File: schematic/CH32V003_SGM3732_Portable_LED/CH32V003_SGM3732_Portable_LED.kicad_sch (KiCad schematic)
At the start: 30 parts, among them J1 USB_C_Receptacle_USB2.0_16P, Q1 CJ2301, Q2 CJ2302, SW1 SW_Push, U1 CH32V003J4M6, U2 ME6211C33M5, U3 SGM3732

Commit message: Update schematic
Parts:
- R_{CC1}: renamed from R7; value 1MΩ -> 5.1kΩ
- R_{CC2}: renamed from R6; value 1MΩ -> 5.1kΩ
- renumbered C3 to C_{LDO_IN}, C4 to C_{LDO_OUT}, C5 to C_{LED_IN}, C6 to C_{LED_OUT}, C2 to C_{MCU}, C1 to C_{P}, D4 to D1, D5 to D2, D6 to D3, D7 to D4, D8 to D5, D3 to D_{LED}, D1 to D_{Latch}, D2 to D_{Power}, L1 to L_{LED}, Q2 to NMOS, Q1 to PMOS, R5 to R_{CTRL}, R3 to R_{Latch}, R2 to R_{N}, R_led to R_{POWER}, R1 to R_{P}, SW1 to SW_{Latch}
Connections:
- net LED renamed Power_LED
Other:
- note added: "Up to 10 LEDs"

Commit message: Update readme and schematic
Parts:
- added R_{Down}: 33kΩ, symbol Device:R
- added R_{Up}: 22kΩ, symbol Device:R
- added SW_{Latch}1: SW_Push, symbol Switch:SW_Push
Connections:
- net 5V: now also R_{Up}.2
- net GND: now also R_{Down}.1, SW_{Latch}1.1
- net ADC: now reaches U1.1 (PD6/PA1)
- net ADC: now also R_{Down}.2, R_{Up}.1
- net Level_Button: now reaches U1.3 (PA2)
- net Level_Button: now also SW_{Latch}1.2
- net Latch_and_Button renamed Mode_Button
- no-connect marks 8 -> 7
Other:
- moved on the sheet: C_{MCU}, C_{P}, D_{Latch}, D_{Power}, J1, NMOS, PMOS, R_{CC1}, R_{CC2}, R_{Latch}, R_{N}, R_{POWER}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

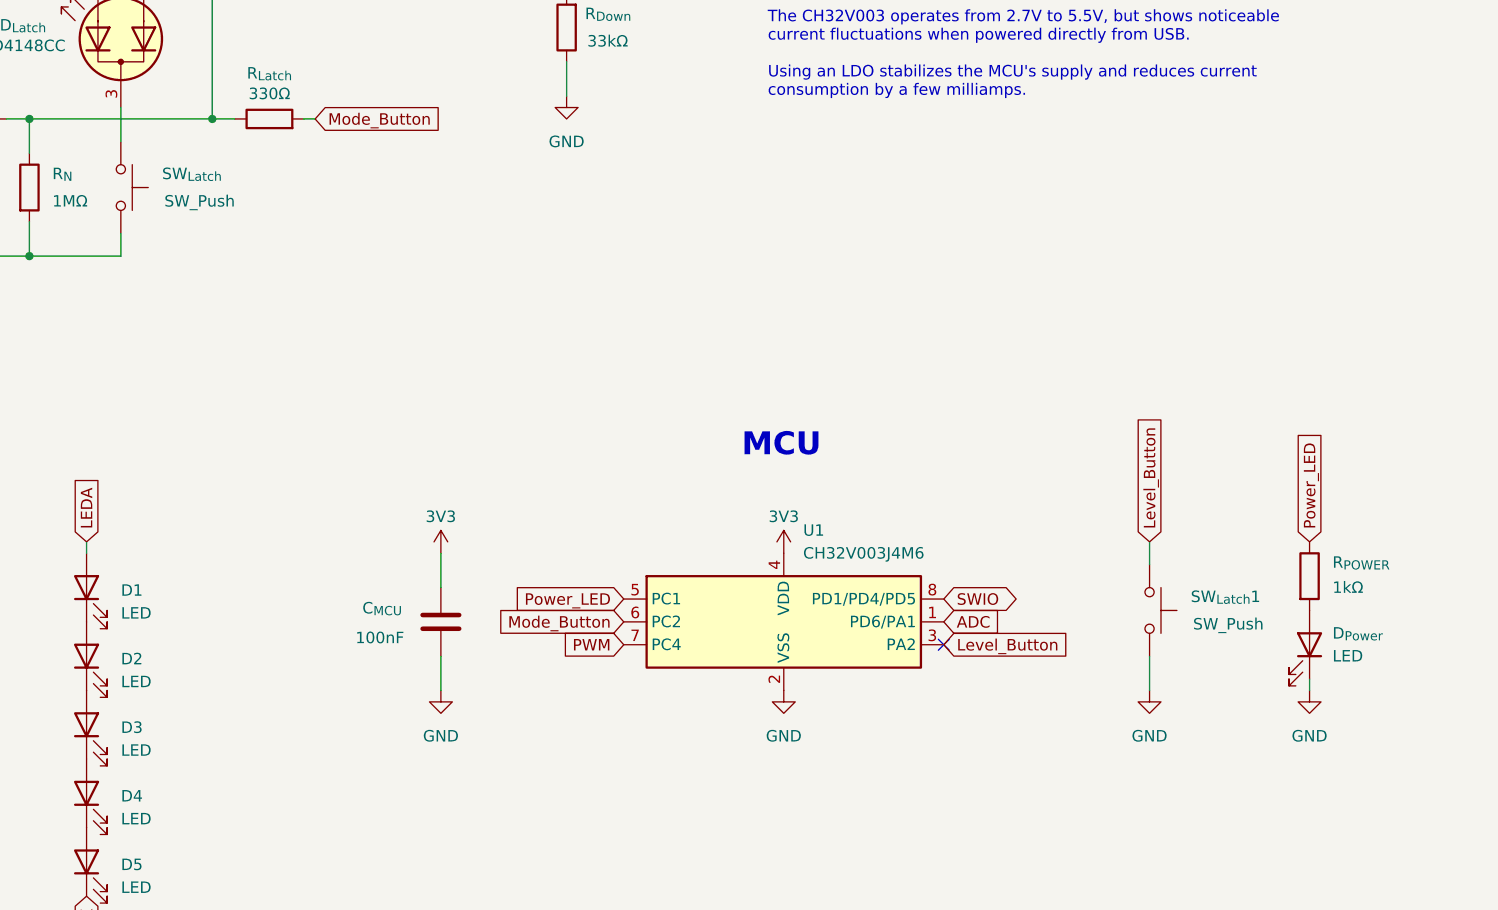
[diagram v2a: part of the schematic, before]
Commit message: Update button names in schematic
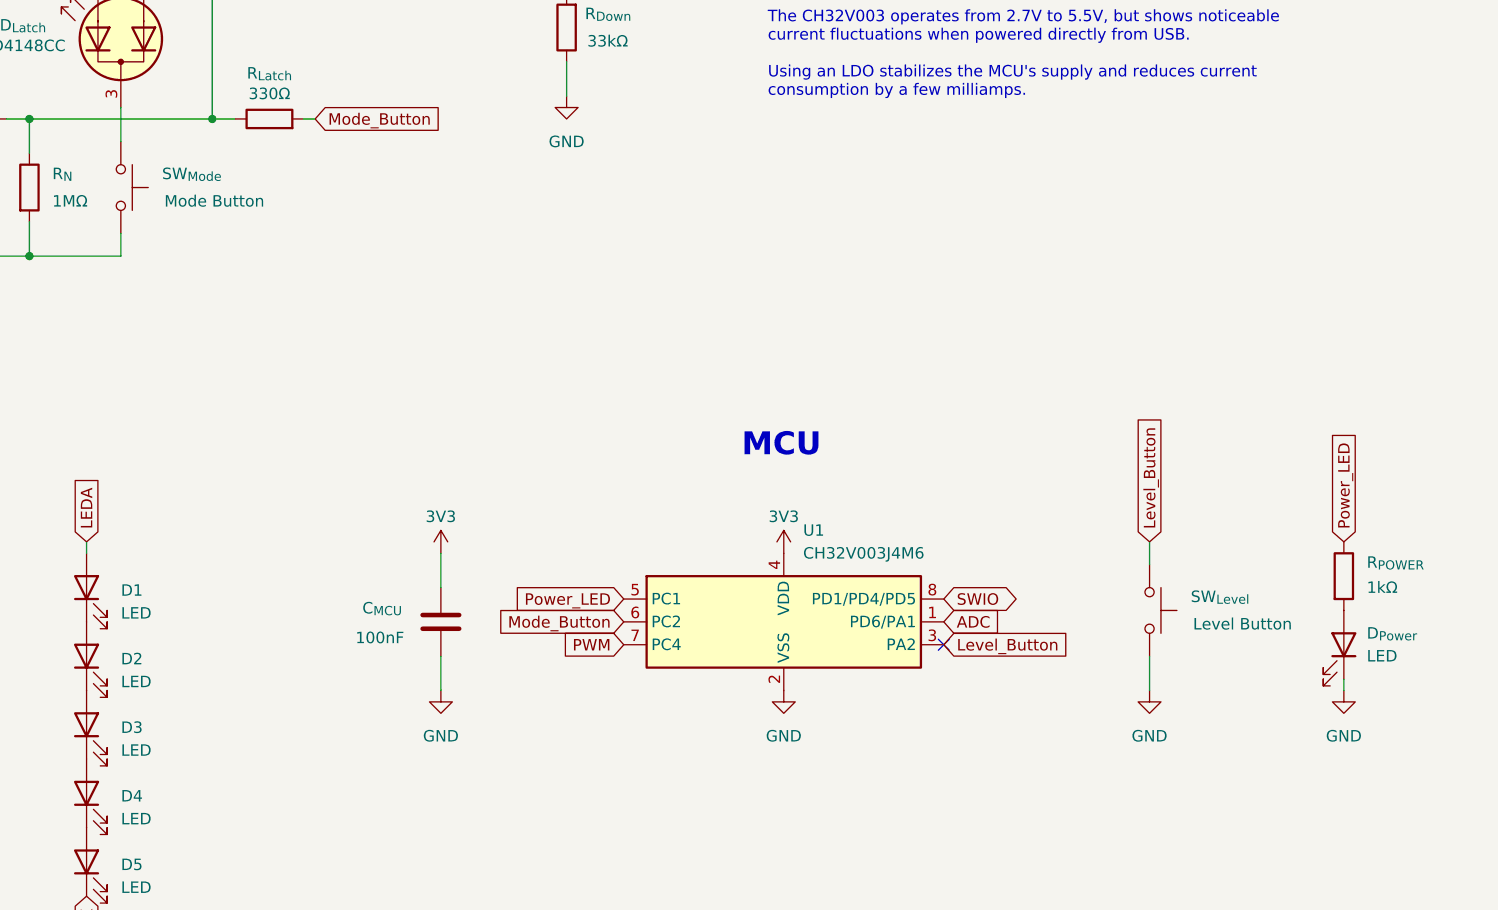
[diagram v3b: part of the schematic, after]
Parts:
- SW_{Level}: renamed from SW_{Latch}1; value SW_Push -> Level Button
- SW_{Mode}: renamed from SW_{Latch}; value SW_Push -> Mode Button
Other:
- moved on the sheet: D_{Power}, R_{POWER}
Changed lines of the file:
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@@
 	(wire
 		(pts
-			(xy 266.7 147.32) (xy 266.7 146.05)
+			(xy 270.51 147.32) (xy 270.51 146.05)
 		)
 		(stroke
@@
 	(global_label "Power_LED"
 		(shape input)
-		(at 266.7 130.81 90)
+		(at 270.51 130.81 90)
 		(fields_autoplaced yes)
 		(effects
@@
 		)
 		(property "Intersheetrefs" "${INTERSHEET_REFS}"
-			(at 266.7 117.7858 90)
+			(at 270.51 117.7858 90)
 			(effects
 				(font
@@
 	(symbol
 		(lib_id "Device:R")
-		(at 266.7 134.62 0)
+		(at 270.51 134.62 0)
 		(unit 1)
 		(exclude_from_sim no)
@@
 		(dnp no)
 		(property "Reference" "R_{POWER}"
-			(at 269.24 133.096 0)
+			(at 273.05 133.096 0)
 			(effects
 				(font
@@
 		)
 		(property "Value" "1kΩ"
-			(at 269.24 135.89 0)
+			(at 273.05 135.89 0)
 			(effects
 				(font
@@
 		)
 		(property "Footprint" ""
-			(at 264.922 134.62 90)
+			(at 268.732 134.62 90)
 			(effects
 				(font
@@
 		)
 		(property "Datasheet" "~"
-			(at 266.7 134.62 0)
+			(at 270.51 134.62 0)
 			(effects
 				(font
@@
 		)
 		(property "Description" ""
-			(at 266.7 134.62 0)
+			(at 270.51 134.62 0)
 			(effects
 				(font
@@
 		(on_board yes)
 		(dnp no)
-		(property "Reference" "SW_{Latch}1"
+		(property "Reference" "SW_{Level}"
 			(at 253.492 136.906 90)
 			(effects
@@
 			)
 		)
-		(property "Value" "SW_Push"
+		(property "Value" "Level Button"
 			(at 253.746 139.954 90)
 			(effects
@@
 			(project "CH32V003_SGM3732_Portable_LED"
 				(path "/06b79fde-572f-4dd7-9a4e-c70d81eb6fb5"
-					(reference "SW_{Latch}1")
+					(reference "SW_{Level}")
 					(unit 1)
 				)
@@
 		(on_board yes)
 		(dnp no)
-		(property "Reference" "SW_{Latch}"
+		(property "Reference" "SW_{Mode}"
 			(at 139.192 89.916 90)
 			(effects
@@
 			)
 		)
-		(property "Value" "SW_Push"
+		(property "Value" "Mode Button"
 			(at 139.446 92.964 90)
 			(effects
@@
 			(project "CH32V003_SGM3732_Portable_LED"
 				(path "/06b79fde-572f-4dd7-9a4e-c70d81eb6fb5"
-					(reference "SW_{Latch}")
+					(reference "SW_{Mode}")
 					(unit 1)
 				)
@@
 	(symbol
 		(lib_id "power:GND")
-		(at 266.7 147.32 0)
+		(at 270.51 147.32 0)
 		(unit 1)
 		(exclude_from_sim no)
@@
 		(fields_autoplaced yes)
 		(property "Reference" "#PWR07"
-			(at 266.7 153.67 0)
+			(at 270.51 153.67 0)
 			(effects
 				(font
@@
 		)
 		(property "Value" "GND"
-			(at 266.7 152.4 0)
+			(at 270.51 152.4 0)
 			(effects
 				(font
@@
 		)
 		(property "Footprint" ""
-			(at 266.7 147.32 0)
+			(at 270.51 147.32 0)
 			(effects
 				(font
@@
 		)
 		(property "Datasheet" ""
-			(at 266.7 147.32 0)
+			(at 270.51 147.32 0)
 			(effects
 				(font
@@
 		)
 		(property "Description" ""
-			(at 266.7 147.32 0)
+			(at 270.51 147.32 0)
 			(effects
 				(font
@@
 	(symbol
 		(lib_id "Device:LED")
-		(at 266.7 142.24 270)
+		(at 270.51 142.24 270)
 		(mirror x)
 		(unit 1)
@@
 		(dnp no)
 		(property "Reference" "D_{Power}"
-			(at 269.24 140.97 90)
+			(at 273.05 140.97 90)
 			(effects
 				(font
@@
 		)
 		(property "Value" "LED"
-			(at 269.24 143.51 90)
+			(at 273.05 143.51 90)
 			(effects
 				(font
@@
 		)
 		(property "Footprint" ""
-			(at 266.7 142.24 0)
+			(at 270.51 142.24 0)
 			(effects
 				(font
@@
 		)
 		(property "Datasheet" "~"
-			(at 266.7 142.24 0)
+			(at 270.51 142.24 0)
 			(effects
 				(font
@@
 		)
 		(property "Description" ""
-			(at 266.7 142.24 0)
+			(at 270.51 142.24 0)
 			(effects
 				(font
